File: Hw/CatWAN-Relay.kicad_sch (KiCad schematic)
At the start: 56 parts, among them J2 INPUTS, J3 OUTPUTS, J4 I2C, J5 Serial, P1 USB_C_Plug_USB2.0, Q1 MMBT2222A, Q2 MMBT2222A, Q3 MMBT2222A, SW1 BOOT, SW2 RESET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

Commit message: feat(hw): Update ESP32-C6 and RFM95 mfr.#
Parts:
- R14, R15: provedor LCSC -> (none)
- U2: manf# RFM95W -> RFM95W-915S2/RFM95W-868S2
- U8: manf# ESP32-C6-WROOM-1-N4 -> ESP32-C6-WROOM-1U-N4; provedor MOUSER -> (none)
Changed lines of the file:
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@@
 		(dnp no)
 		(property "Reference" "U2"
-			(at 153.67 140.97 0)
+			(at 153.67 125.984 0)
 			(effects
 				(font
@@
 			)
 		)
-		(property "manf#" "RFM95W"
+		(property "manf#" "RFM95W-915S2/RFM95W-868S2"
 			(at 153.67 140.97 0)
 			(effects
@@
 		(dnp no)
 		(property "Reference" "R9"
-			(at 276.86 35.56 0)
+			(at 279.654 33.782 0)
 			(effects
 				(font
 					(size 1.27 1.27)
 				)
-				(hide yes)
 			)
 		)
 		(property "Value" "120R"
-			(at 276.86 35.56 0)
+			(at 280.162 35.56 0)
 			(effects
 				(font
 					(size 1.27 1.27)
 				)
-				(hide yes)
 			)
 		)
@@
 		(dnp no)
 		(property "Reference" "R11"
-			(at 259.08 36.83 0)
+			(at 262.382 34.798 0)
 			(effects
 				(font
 					(size 1.27 1.27)
 				)
-				(hide yes)
 			)
 		)
 		(property "Value" "120R"
-			(at 259.08 36.83 0)
+			(at 262.636 36.83 0)
 			(effects
 				(font
 					(size 1.27 1.27)
 				)
-				(hide yes)
 			)
 		)
@@
 			)
 		)
-		(property "Datasheet" ""
+		(property "Datasheet" "https://www.espressif.com/sites/default/files/documentation/esp32-c6-wroom-1_wroom-1u_datasheet_en.pdf"
 			(at 159.512 35.814 0)
 			(effects
@@
 			)
 		)
-		(property "manf#" "ESP32-C6-WROOM-1-N4"
+		(property "manf#" "ESP32-C6-WROOM-1U-N4"
 			(at 145.796 15.24 0)
 			(effects
@@
 			)
 		)
-		(property "provedor" "MOUSER"
-			(at 144.78 50.8 0)
-			(effects
-				(font
-					(size 1.27 1.27)
-				)
-				(hide yes)
-			)
-		)
 		(property "Proveedor" "MOUSER"
 			(at 144.78 50.8 0)
@@
 			)
 		)
-		(property "provedor" "LCSC"
-			(at 48.26 147.32 0)
-			(effects
-				(font
-					(size 1.27 1.27)
-				)
-				(hide yes)
-			)
-		)
 		(property "Proveedor" "LCSC"
 			(at 48.26 147.32 0)
@@
 			(at 48.26 149.86 0)
 			(effects
-				(font
-					(size 1.27 1.27)
-				)
-				(hide yes)
-			)
-		)
-		(property "provedor" "LCSC"
-			(at 48.26 149.86 0)
-			(effects

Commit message: feat: Boot and Reset buttons footprint changed
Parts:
- SW1, SW2: footprint Button_Switch_SMD:SW_SPST_TL3342 -> Button_Switch_SMD:SW_Push_SPST_NO_Alps_SKRK; LCSC# C318889 -> C455281; Proveedor JLCPCB -> LCSC; manf# TL3342F160QG -> (none)
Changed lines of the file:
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@@
 			)
 		)
-		(property "Footprint" "Button_Switch_SMD:SW_SPST_TL3342"
+		(property "Footprint" "Button_Switch_SMD:SW_Push_SPST_NO_Alps_SKRK"
 			(at 199.39 101.6 0)
 			(effects
@@
 			)
 		)
-		(property "manf#" "TL3342F160QG"
+		(property "manf#" ""
 			(at 199.39 106.68 0)
 			(effects
@@
 			)
 		)
-		(property "LCSC#" "C318889"
+		(property "LCSC#" "C455281"
 			(at 199.39 106.68 0)
 			(effects
@@
 			)
 		)
-		(property "Proveedor" "JLCPCB"
+		(property "Proveedor" "LCSC"
 			(at 199.39 106.68 0)
 			(effects
@@
 			)
 		)
-		(property "Footprint" "Button_Switch_SMD:SW_SPST_TL3342"
+		(property "Footprint" "Button_Switch_SMD:SW_Push_SPST_NO_Alps_SKRK"
 			(at 176.53 100.33 0)
 			(effects
@@
 			)
 		)
-		(property "manf#" "TL3342F160QG"
+		(property "manf#" ""
 			(at 176.53 105.41 0)
 			(effects
@@
 			)
 		)
-		(property "LCSC#" "C318889"
+		(property "LCSC#" "C455281"
 			(at 176.53 105.41 0)
 			(effects
@@
 			)
 		)
-		(property "Proveedor" "JLCPCB"
+		(property "Proveedor" "LCSC"
 			(at 176.53 105.41 0)
 			(effects

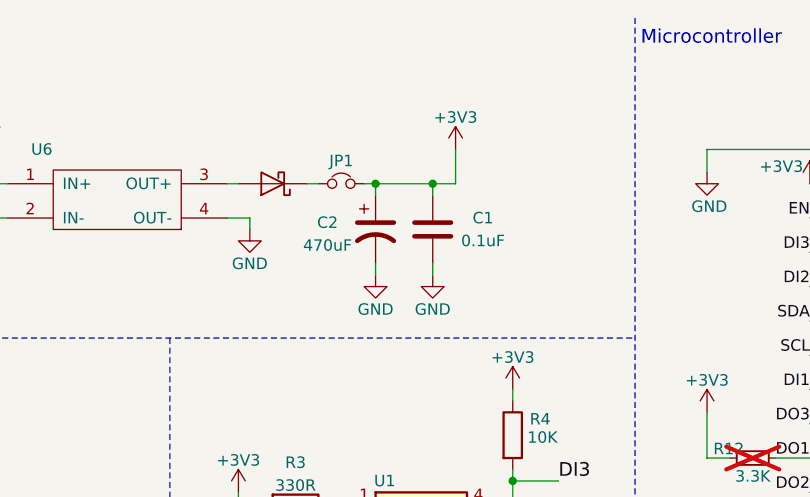
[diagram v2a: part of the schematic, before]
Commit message: Feat: floorplan added
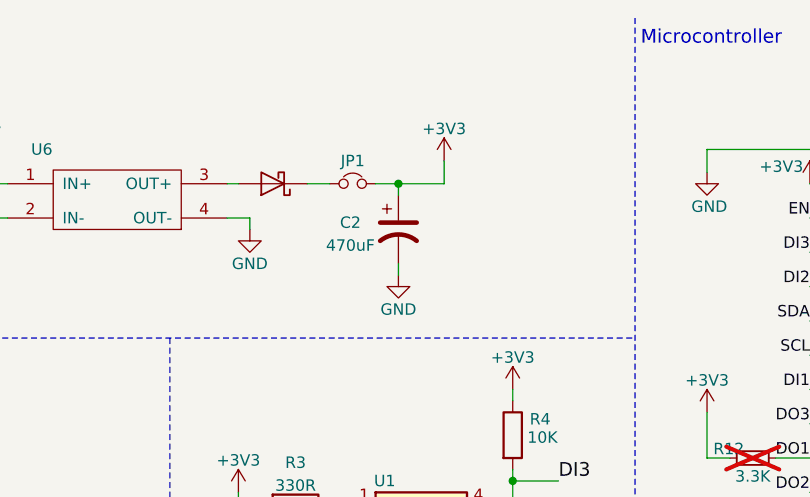
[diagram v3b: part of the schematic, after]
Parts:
- removed C1: 0.1uF, Capacitor_SMD:C_0603_1608Metric, symbol CatWAN-Relay-rescue:C-agroin-rescue
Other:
- moved on the sheet: C2, JP1

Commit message: feat: files_modified, _pro, _pcb & _sch
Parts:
- removed J4: I2C, Connector_PinHeader_2.54mm:PinHeader_1x04_P2.54mm_Vertical, symbol CatWAN-Relay-rescue:Conn_01x04-agroin-rescue
- added J1: Conn_01x01, Connector_PinHeader_2.54mm:PinHeader_1x01_P2.54mm_Vertical, symbol Connector_Generic:Conn_01x01
- added J4: I2C, Connector_PinHeader_2.54mm:PinHeader_1x06_P2.54mm_Vertical, symbol Connector_Generic:Conn_01x06
- D7: value Rx -> SS0_LED; LCSC# C205442 -> C130114; manf# APT2012SGC -> AP2012EC
- U8: footprint PCM_Espressif:ESP32-C6-WROOM-1U -> Espressif:ESP32-C6-WROOM-1U
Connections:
- net +3V3: now also J4.1 (Pin_1)
- net GND: now also J4.6 (Pin_6)
- net SCL: now also J4.3 (Pin_3)
- net SDA: now also J4.2 (Pin_2)
- net RX_LED renamed SS1
- net SS1: now also J1.1 (Pin_1), J4.5 (Pin_5)
- net SS renamed SS0
